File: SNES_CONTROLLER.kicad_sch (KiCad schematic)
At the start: 29 parts, among them J1 Screw_Terminal_01x06, J2 Screw_Terminal_01x12, J3 Screw_Terminal_01x12, U1 4021, U2 4021

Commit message: Add BOM information to project
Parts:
- C1, C2: Digikey P/N (none) -> 56-K103K10X7RF5UL2CT-ND; Farnell P/N (none) -> 4209313; Mfr. P/N (none) -> K103K10X7RF5UL2; Mouser P/N (none) -> 594-K103K10X7RF5UL2
- J1, J2, J3: Digikey P/N (none) -> 277-2518-ND; Farnell P/N (none) -> 2072377; Mfr. P/N (none) -> 1792863; Mouser P/N (none) -> 651-1792863
- R1, R10, R11, R12, R13, R14, R15, R16, R17, R18, R19, R2, R3, R4, R5, R6, R7, R8, R9: Digikey P/N (none) -> 13-MFR-25FRF52-10KCT-ND; Farnell P/N (none) -> 3951796; Mfr. P/N (none) -> MFR-25FRF52-10K; Mouser P/N (none) -> 603-MFR-25FRF5210K
- U1, U2: Digikey P/N (none) -> 296-2040-5-ND; Farnell P/N (none) -> 3120813; Mfr. P/N (none) -> CD4021BE; Mouser P/N (none) -> 595-CD4021BE

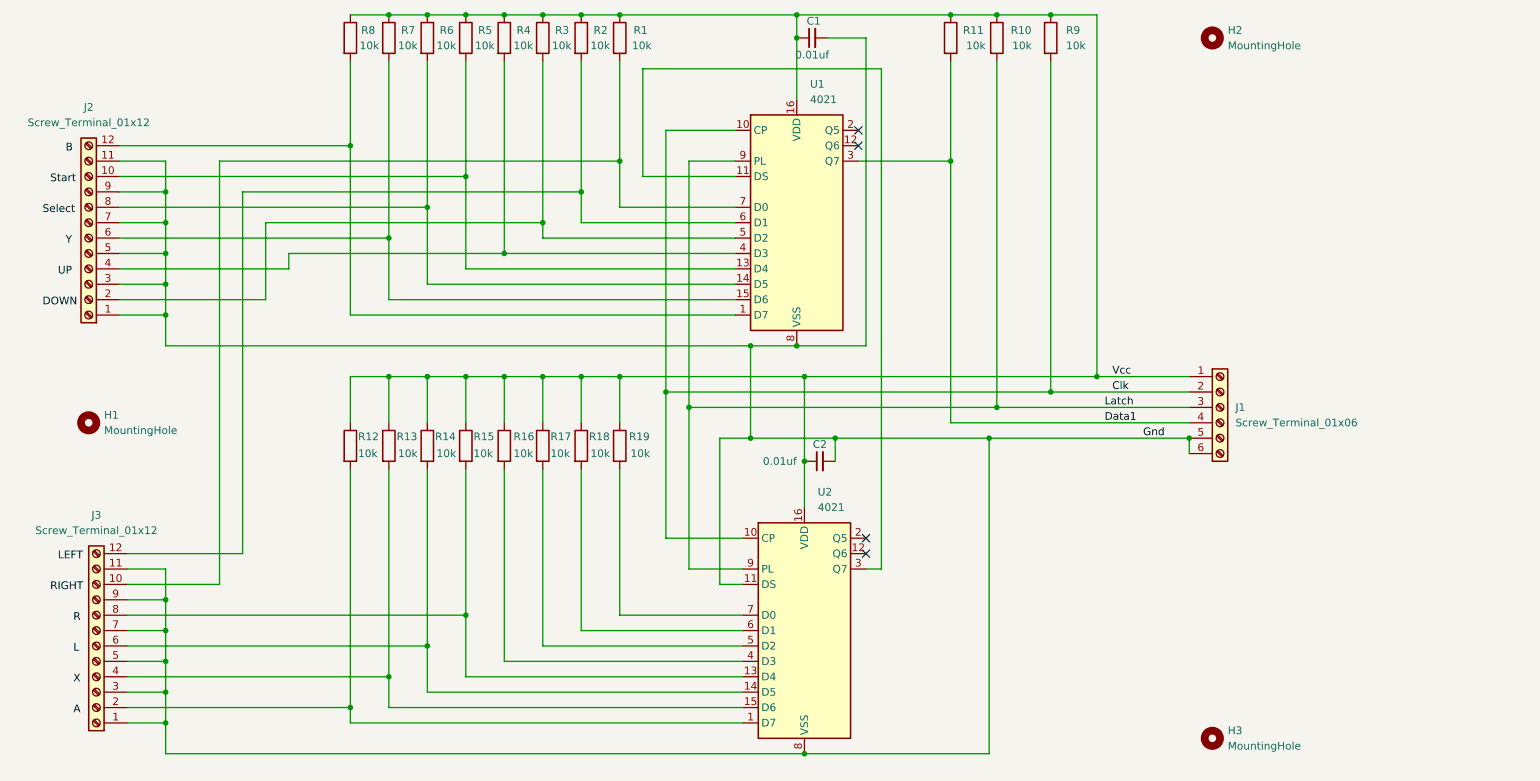
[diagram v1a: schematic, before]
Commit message: Add IC sockets to project
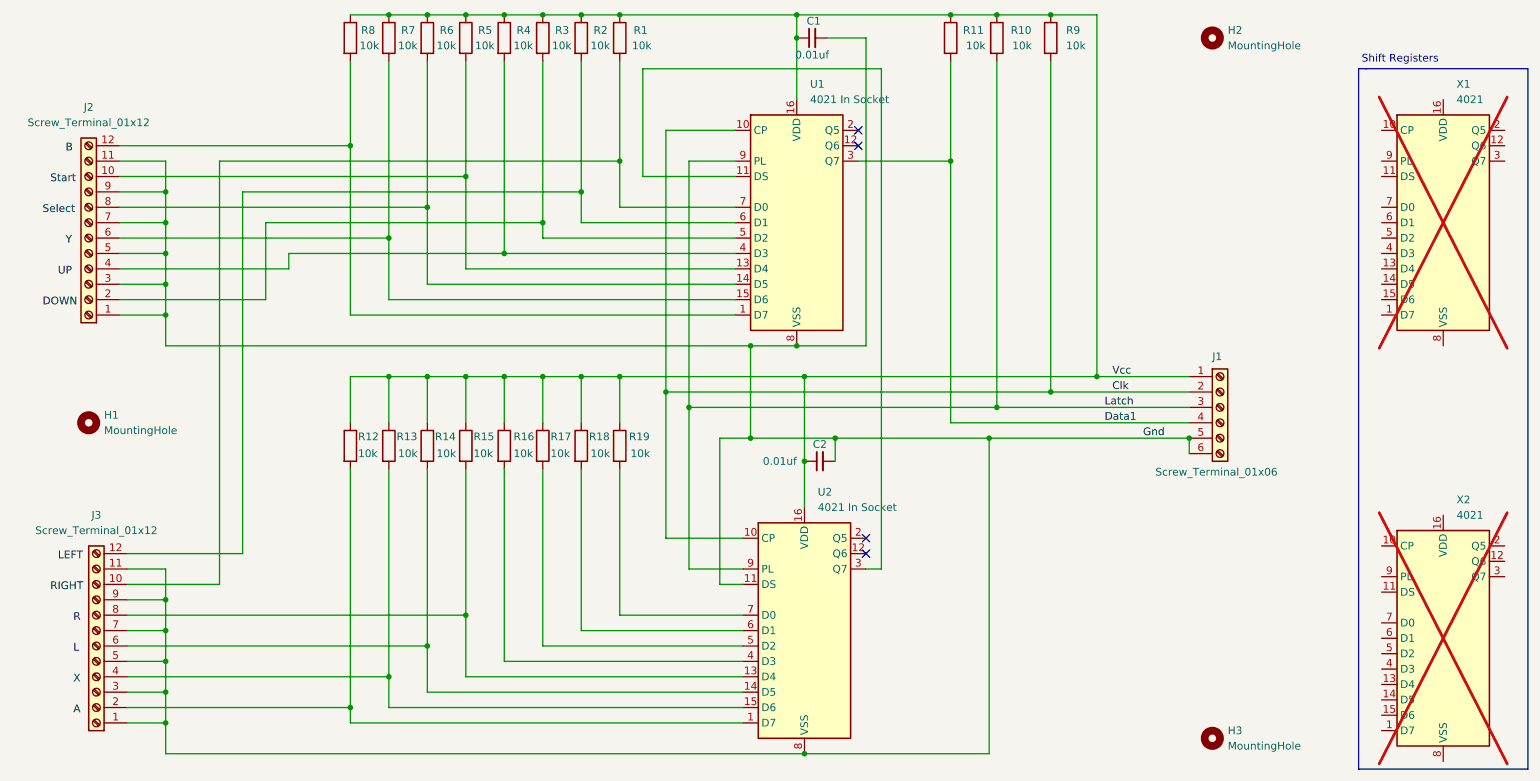
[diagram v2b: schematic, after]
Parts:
- added X1: 4021, Package_DIP:DIP-16_W7.62mm, symbol 4xxx:4021
- added X2: 4021, Package_DIP:DIP-16_W7.62mm_Socket, symbol 4xxx:4021
- U1, U2: value 4021 -> 4021 In Socket; footprint Package_DIP:DIP-16_W7.62mm -> Package_DIP:DIP-16_W7.62mm_Socket; Digikey P/N 296-2040-5-ND -> 17-2485264-3-ND; Farnell P/N 3120813 -> 4575164; Mfr. P/N CD4021BE -> 2485264-3; Mouser P/N 595-CD4021BE -> 571-2485264-3
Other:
- note added: "Shift Registers"
